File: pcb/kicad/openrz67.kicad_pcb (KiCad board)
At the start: 2 copper layers, 48 x 22 mm, 57 parts, among them J1 GPIO header, U1 ESP32-C3FH4, U2 TPS63031DSKR, U3 BQ25185DLHR, U4 S4B-XH-A(LF)(SN), U5 TLP172AM, U6 TLP172AM, X1 40MHz, X2 32.768kHz

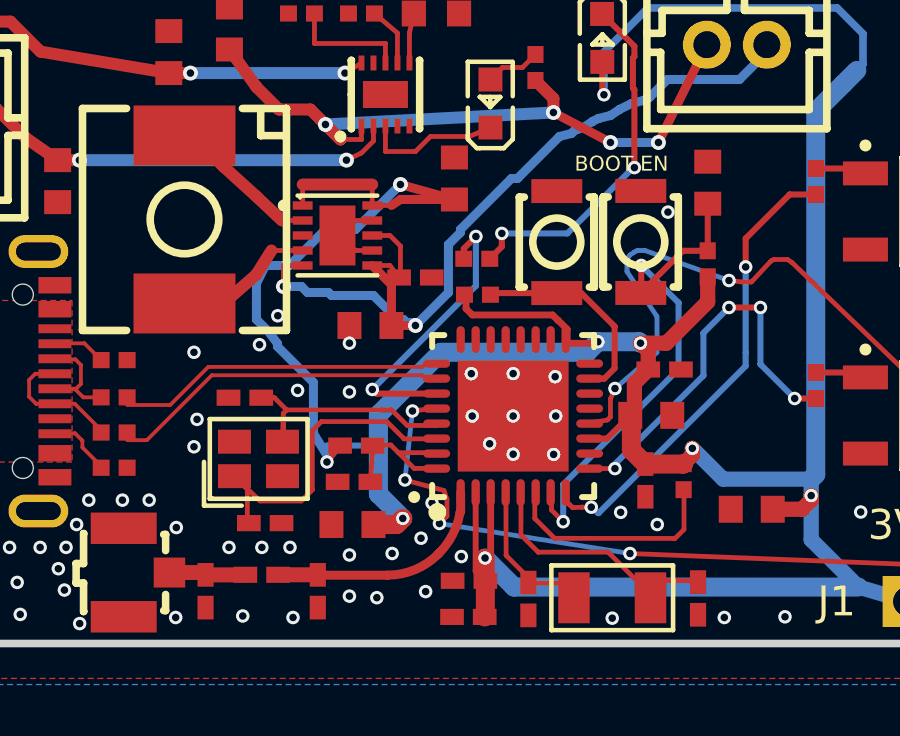
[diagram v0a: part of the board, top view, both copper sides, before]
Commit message: PCB: routing pass — U2 EP vias + solid GND, VCC feed off U2 pad, GPIO21 jog away from LNA_IN
- U2 exposed pad: 4 GND vias (0.45/0.25); U2 and USB1 pads 1/12 solid zone
  connect, starved_thermal warnings gone
- B.Cu VCC feed from U2 output routed around the west side of U2 instead of
  under its pad; SW1/SW2 pad exits 0.254 mm
- GPIO21 F.Cu jog next to U1 pin 1 (LNA_IN) moved 0.75 mm west (0.21 -> 0.79 mm
  to the RF trace); two GND stitching vias relocated
- DRC: 0 errors, 0 unconnected; B.Cu ground under U1 keeps its channel
- README: via 0.45/0.25, warnings table, changelog; out/ regenerated
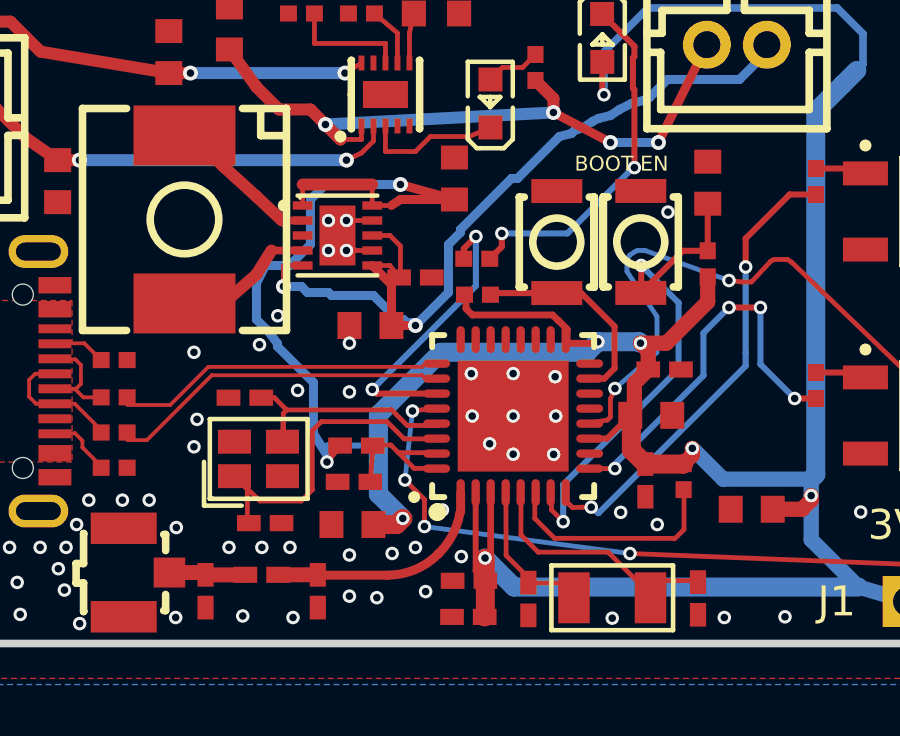
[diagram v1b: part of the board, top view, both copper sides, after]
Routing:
- net VCC: track 116.6 -> 117.5 mm
- net GND: vias 74 -> 78
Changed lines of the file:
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@@
 			)
 		)
+		(zone_connect 2)
 		(attr smd)
 		(duplicate_pad_numbers_are_jumpers no)
@@
 			(layers "F.Cu" "F.Mask" "F.Paste")
 			(net "GND")
+			(zone_connect 2)
 		)
 		(pad "2" smd rect
@@
 			(layers "F.Cu" "F.Mask" "F.Paste")
 			(net "GND")
+			(zone_connect 2)
 		)
 		(pad "13" thru_hole oval
@@
 	)
 	(via
-		(at 138.1865 108.4905)
+		(at 138 108.8)
 		(size 0.45)
 		(drill 0.25)
@@
 	)
 	(via
+		(at 135.7 98.9)
+		(size 0.45)
+		(drill 0.25)
+		(layers "F.Cu" "B.Cu")
+		(net "GND")
+	)
+	(via
 		(at 121.3715 101.735)
 		(size 0.45)
@@
 	)
 	(via
-		(at 138.5525 107.3195)
+		(at 135.1 98.9)
+		(size 0.45)
+		(drill 0.25)
+		(layers "F.Cu" "B.Cu")
+		(net "GND")
+	)
+	(via
+		(at 138.9 107.55)
 		(size 0.45)
 		(drill 0.25)
@@
 	)
 	(via
+		(at 135.1 97.9)
+		(size 0.45)
+		(drill 0.25)
+		(layers "F.Cu" "B.Cu")
+		(net "GND")
+	)
+	(via
 		(at 150.3175 111.11)
 		(size 0.45)
@@
 	)
 	(via
+		(at 135.7 97.9)
+		(size 0.45)
+		(drill 0.25)
+		(layers "F.Cu" "B.Cu")
+		(net "GND")
+	)
+	(via
 		(at 121.219 102.7)
 		(size 0.45)
@@
 	)
 	(segment
+		(start 134.5 97.2)
+		(end 134.5 98.7)
+		(width 0.3)
+		(layer "B.Cu")
+		(net "VCC")
+	)
+	(segment
 		(start 136.764 107.018)
 		(end 136.764 104.3765)
@@
 	)
 	(segment
-		(start 137.5 96.7)
-		(end 136 98.2)
+		(start 134.6 103.3)
+		(end 134.6 105)
 		(width 0.3)
 		(layer "B.Cu")
@@
 	)
 	(segment
-		(start 134.6 103.3)
-		(end 134.6 105)
+		(start 137.5 96.7)
+		(end 135 96.7)
 		(width 0.3)
 		(layer "B.Cu")
@@
 	)
 	(segment
-		(start 136 98.2)
-		(end 135 98.2)
-		(width 0.3)
-		(layer "B.Cu")
-		(net "VCC")
-	)
-	(segment
 		(start 134.6 105)
 		(end 135.1 105.8)
@@
 	)
 	(segment
-		(start 135 98.2)
-		(end 133.8 99.4)
+		(start 135 96.7)
+		(end 134.5 97.2)
 		(width 0.3)
 		(layer "B.Cu")
@@
 	)
 	(segment
+		(start 134.5 98.7)
+		(end 133.8 99.4)
+		(width 0.3)
+		(layer "B.Cu")
+		(net "VCC")
+	)
+	(segment
 		(start 129.826 104.0495)
 		(end 131.095 102.78)
@@
 		(start 134.24 97.9)
 		(end 133.55 97.9)
-		(width 0.16)
+		(width 0.254)
 		(layer "F.Cu")
 		(net "SW2")
@@
 		(start 134.24 98.9)
 		(end 133.199999 98.9)
-		(width 0.16)
+		(width 0.254)
 		(layer "F.Cu")
 		(net "SW1")
@@
 	)
 	(segment
-		(start 138.95 106.9)
-		(end 139.05 107.2)
-		(width 0.16)
-		(layer "F.Cu")
-		(net "GPIO21")
-	)
-	(segment
 		(start 138.7 104.15)
 		(end 137.9 104.25)
@@
 	)
 	(segment
-		(start 139.05 107.2)
-		(end 139.05 107.75)
+		(start 138.3 107.2)
+		(end 138.3 108.1)
 		(width 0.16)
 		(layer "F.Cu")
@@
 	)
 	(segment
-		(start 139.05 107.75)
-		(end 138.8 108)
-		(width 0.16)
-		(layer "F.Cu")
-		(net "GPIO21")
-	)
-	(segment
 		(start 137.65 106.55)
-		(end 138.95 106.9)
+		(end 138.3 107.2)
 		(width 0.16)
 		(layer "F.Cu")
@@
 	)
 	(via
-		(at 138.8 108)
+		(at 137.65 106.55)
 		(size 0.45)
 		(drill 0.25)
@@
 	)
 	(via
-		(at 137.65 106.55)
+		(at 138.3 108.1)
 		(size 0.45)
 		(drill 0.25)
@@
 	)
 	(segment
-		(start 138.8 108)
+		(start 138.3 108.1)
 		(end 145.15 109)
 		(width 0.16)

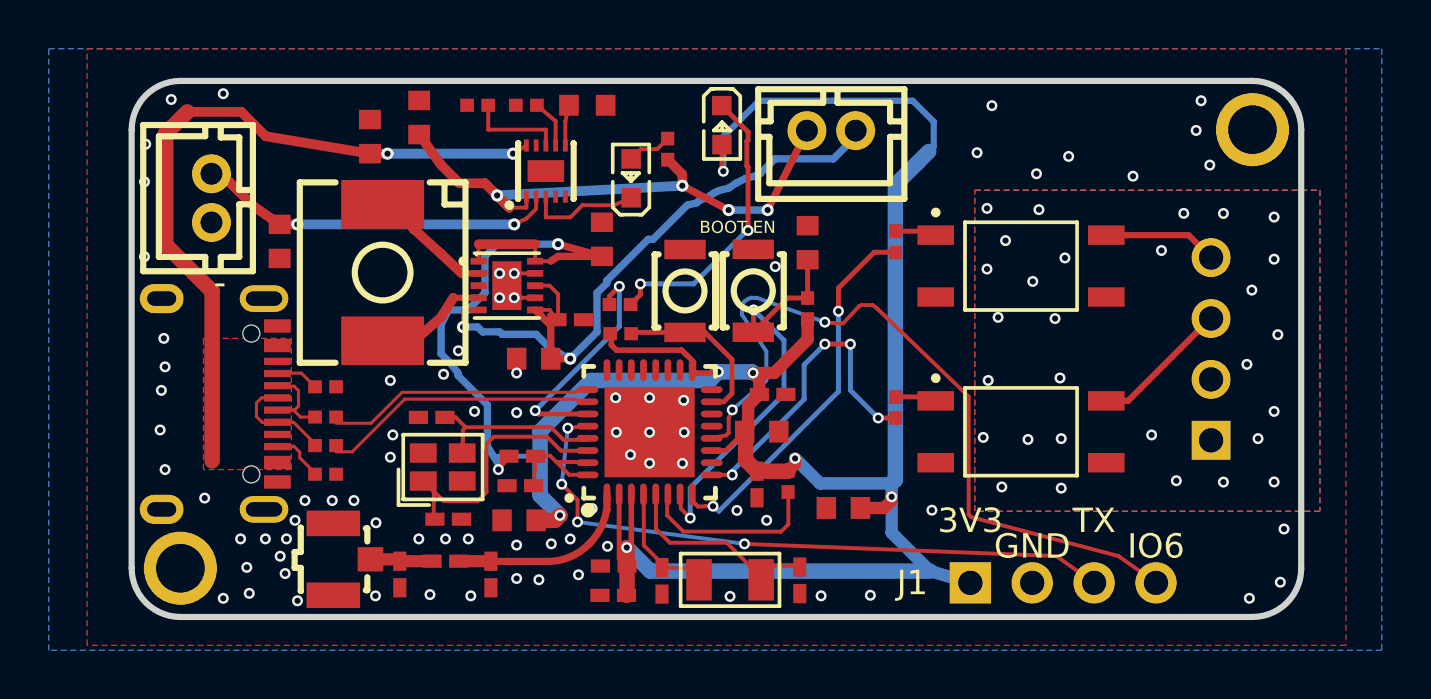
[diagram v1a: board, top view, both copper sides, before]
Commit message: PCB: review fixes — C23 at U2 VIN, GND necks opened, GPIO21 single B.Cu run, U3 EP vias
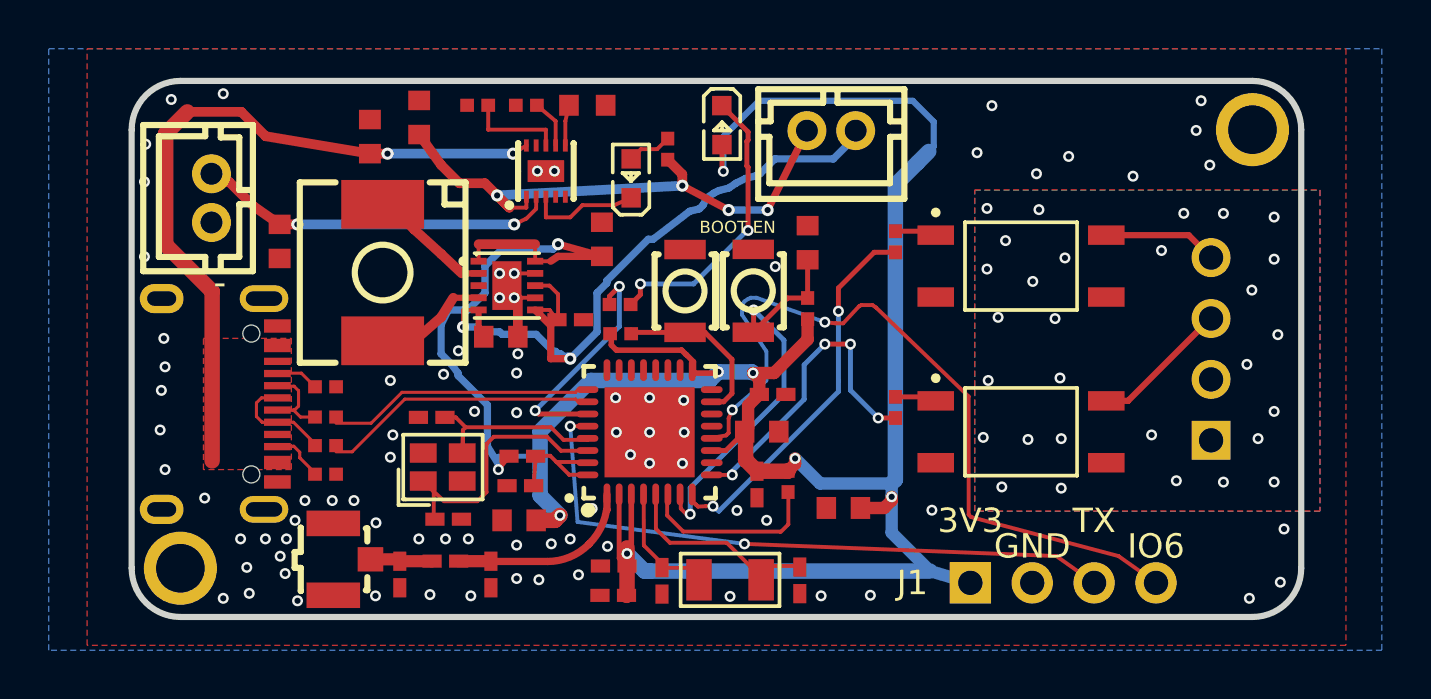
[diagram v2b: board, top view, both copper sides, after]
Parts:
- moved C23 1.62 mm to (135.2, 100.5), turned to 180 degrees
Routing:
- net GND: track 1.40 -> 2.90 mm, vias 78 -> 81
- net SW_SYS: track 29.1 -> 30.3 mm
- net GPIO21: track 26.6 -> 26.3 mm, vias 4 -> 2

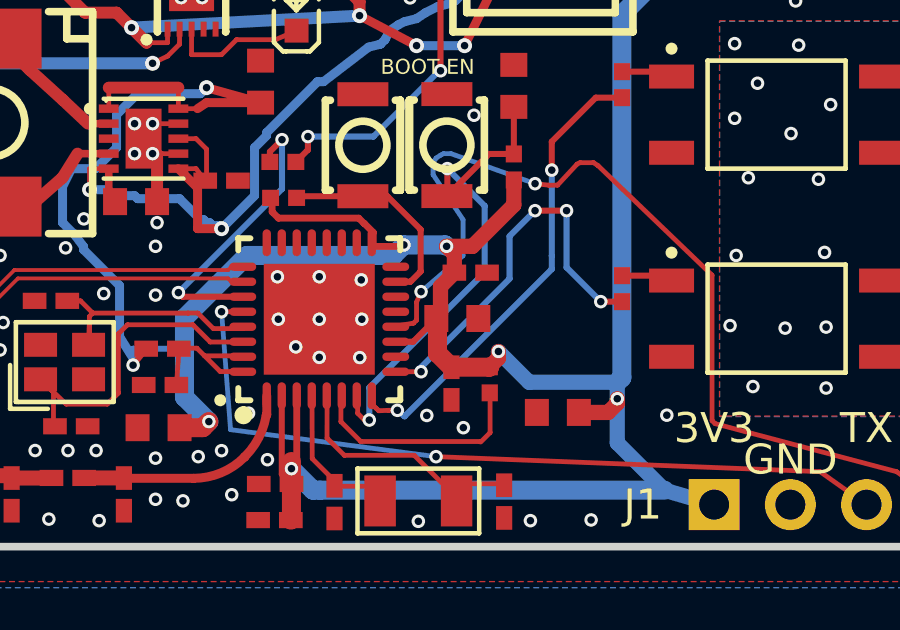
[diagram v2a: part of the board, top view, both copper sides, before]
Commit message: PCB: R23 10k pull-up on GPIO8 (strapping pin was floating); C29 +0.55 mm, GPIO6 via moved, VCC artery on x 25.709
GPIO8 needs to be high for Joint Download Boot and has no internal pull;
rev 1 and the ordered rev 2 leave it floating behind a no-connect flag.
Also adds the 2026-09-10 design review and its adversarial counter-read
under notes/. VDD_SPI 1 uF not added: no room on the top side (README).
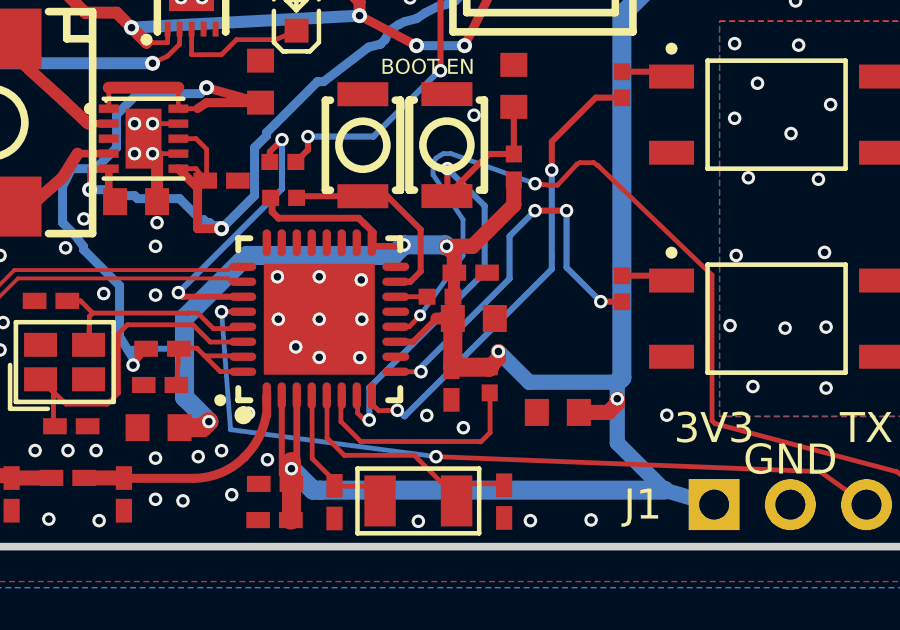
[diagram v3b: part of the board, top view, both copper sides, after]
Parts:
- added R23: 10kΩ, openrz67:R0402, F.Cu at (145.3, 103.7)
- moved C29 0.55 mm to (146.4, 104.4)
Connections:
- U1 pad 14: unconnected-(U1-GPIO8-Pad14) -> GPIO8
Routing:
- net GPIO8: track 0.00 -> 1.04 mm

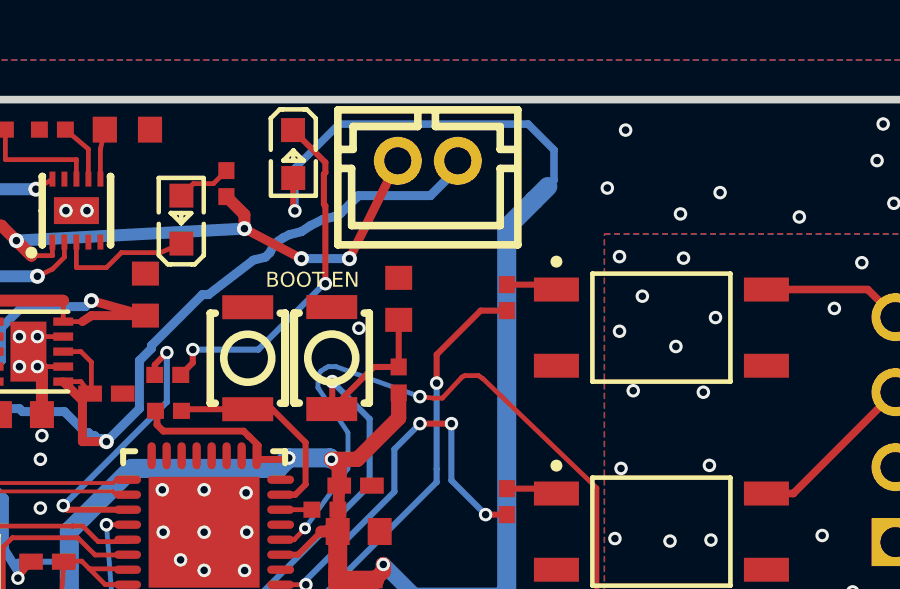
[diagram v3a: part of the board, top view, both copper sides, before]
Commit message: PCB rev 3: battery voltage sense on GPIO3, S2 relay moved to GPIO6
R24/R25 1 MΩ + C32 100 nF under S3 divide SW_SYS (switched cell voltage; BQ25185
SYS voltage on USB) into GPIO3/ADC1_CH3 through the old S2_DRV copper. S2_DRV now
comes from GPIO6 (pin 12), fed off the existing GPIO6 track at (150.55, 99.3), so
J1 pin 4 carries the S2 drive. Every other spare pin was boxed in; BAT+ was
unreachable from U1. DRC 0 errors / 0 unconnected (two new courtyard warnings),
ERC unchanged, title block rev 3. Firmware todo for rev 3 in pcb/kicad/README.md;
src/ still targets rev 2.
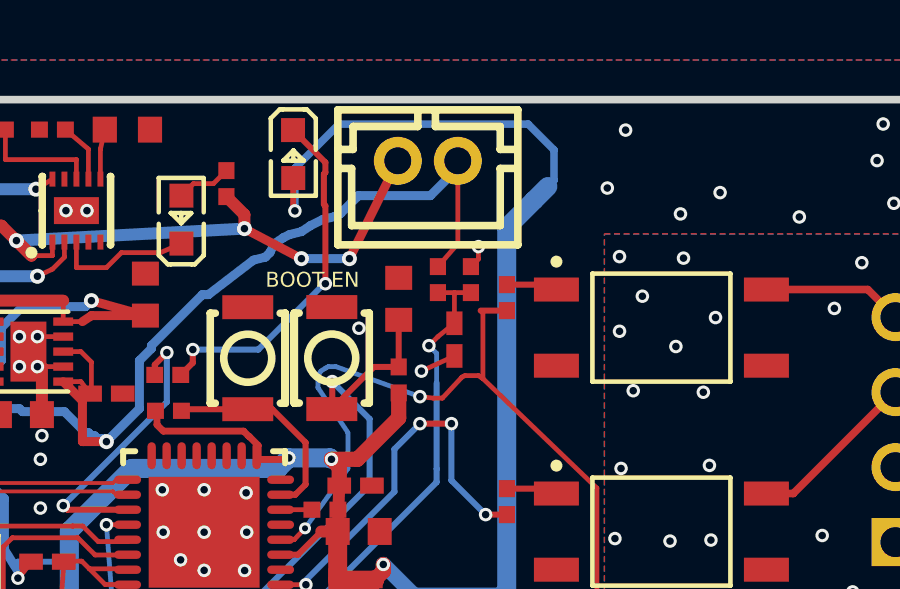
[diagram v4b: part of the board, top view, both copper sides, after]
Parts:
- added C32: 100nF, openrz67:C0402, F.Cu at (149.6, 98.0)
- added R24: 1MΩ, openrz67:R0402, F.Cu at (149.1, 96.0)
- added R25: 1MΩ, openrz67:R0402, F.Cu at (150.2, 96.0)
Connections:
- J1 pad 4: GPIO6 -> S2_DRV
- U1 pad 12: GPIO6 -> S2_DRV
- U1 pad 8: S2_DRV -> VBAT_SENSE
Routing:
- net GPIO6: track 31.4 -> 0.00 mm, vias 2 -> 0
- net S2_DRV: track 15.7 -> 34.6 mm
- net VBAT_SENSE: track 0.00 -> 16.4 mm, vias 0 -> 2
- net SW_SYS: track 30.3 -> 34.1 mm
- net GND: track 2.90 -> 4.88 mm, vias 81 -> 83

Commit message: PCB rev 3: J1 shrinks to 1x3 (3V3, GND, TX); GPIO6 track to the old pin 4 and IO6 silk removed
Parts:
- J1: footprint openrz67:PinHeader_1x04_P2.54mm_Vertical -> openrz67:PinHeader_1x03_P2.54mm_Vertical
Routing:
- net S2_DRV: track 34.6 -> 16.1 mm
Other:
- board text removed: "IO6"
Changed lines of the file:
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@@
 		)
 	)
-	(footprint "openrz67:PinHeader_1x04_P2.54mm_Vertical"
+	(footprint "openrz67:PinHeader_1x03_P2.54mm_Vertical"
 		(layer "F.Cu")
 		(at 154.42 110.6 90)
-		(descr "Through hole straight pin header, 1x04, 2.54mm pitch, single row")
-		(tags "Through hole pin header THT 1x04 2.54mm single row")
+		(descr "Through hole straight pin header, 1x03, 2.54mm pitch, single row")
+		(tags "Through hole pin header THT 1x03 2.54mm single row")
 		(property "Reference" "J1"
 			(at 0 -2.38 0)
@@
 		)
 		(property "Value" "GPIO header"
-			(at 0 10 0)
+			(at 0 7.5 0)
 			(layer "F.Fab")
 			(effects
@@
 			)
 		)
-		(property "Description" "1x4 2.54 mm pin header, not populated by the assembler"
+		(property "Description" "1x3 2.54 mm pin header, not populated by the assembler"
 			(at 0 0 0)
 			(layer "F.Fab")
@@
 		(fp_rect
 			(start -1.77 -1.77)
-			(end 1.77 9.39)
+			(end 1.77 6.85)
 			(stroke
 				(width 0.05)
@@
 		(fp_line
 			(start 1.27 -1.27)
-			(end 1.27 8.89)
+			(end 1.27 6.35)
 			(stroke
 				(width 0.1)
@@
 		)
 		(fp_line
-			(start 1.27 8.89)
-			(end -1.27 8.89)
+			(start 1.27 6.35)
+			(end -1.27 6.35)
 			(stroke
 				(width 0.1)
@@
 		)
 		(fp_line
-			(start -1.27 8.89)
+			(start -1.27 6.35)
 			(end -1.27 -0.635)
 			(stroke
@@
 		)
 		(fp_text user "${REFERENCE}"
-			(at 0 3.81 90)
+			(at 0 2.54 90)
 			(layer "F.Fab")
 			(effects
@@
 			(net "GPIO21")
 		)
-		(pad "4" thru_hole circle
-			(at 0 7.62 90)
-			(size 1.7 1.7)
-			(drill 1)
-			(layers "*.Cu" "*.Mask")
-			(remove_unused_layers no)
-			(net "S2_DRV")
-		)
 		(embedded_fonts no)
-		(model "${KICAD10_3DMODEL_DIR}/Connector_PinHeader_2.54mm.3dshapes/PinHeader_1x04_P2.54mm_Vertical.step"
+		(model "${KICAD10_3DMODEL_DIR}/Connector_PinHeader_2.54mm.3dshapes/PinHeader_1x03_P2.54mm_Vertical.step"
 			(offset
 				(xyz 0 0 0)
@@
 		)
 	)
-	(gr_text "IO6"
-		(at 162.04 109.1 0)
-		(layer "F.SilkS")
-		(effects
-			(font
-				(size 1 1)
-				(thickness 0.15)
-			)
-		)
-	)
 	(gr_text "-"
 		(at 123.354 98.9025 0)
@@
 	)
 	(segment
-		(start 154.35 102.95)
-		(end 154.35 107.8)
-		(width 0.16)
-		(layer "F.Cu")
-		(net "S2_DRV")
-	)
-	(segment
 		(start 144.257 104.669)
 		(end 144.62 104.29)
@@
 	)
 	(segment
-		(start 154.35 107.8)
-		(end 154.45 107.9)
-		(width 0.16)
-		(layer "F.Cu")
-		(net "S2_DRV")
-	)
-	(segment
 		(start 149.85 99.25)
 		(end 149.95 99.2)
@@
 		(layer "F.Cu")
 		(net "S2_DRV")
-	)
-	(segment
-		(start 150.55 99.3)
-		(end 154.35 102.95)
-		(width 0.16)
-		(layer "F.Cu")
-		(net "S2_DRV")
-	)
-	(segment
-		(start 154.45 107.9)
-		(end 160.5 109.5)
-		(width 0.16)
-		(layer "F.Cu")
-		(net "S2_DRV")
-	)
-	(segment
-		(start 160.5 109.5)
-		(end 162.05 110.6)
-		(width 0.16)
-		(layer "F.Cu")
-		(net "S2_DRV")

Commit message: PCB rev 3: reverse-battery P-FET Q3, C24 at the buck-boost output, EP paste windows, 0.8 mm RF line, review notes
Review round 2026-09-25 (pcb/kicad/notes/review-2026-09-25.md):
- Q3 AO3401A (SOT-23, C15127) between BAT1 pin 1 (new net BAT_CELL) and BAT+;
  gate to GND. VBUS moved to B.Cu under it; BAT+ rerouted west of L3 pad 1.
- C24 to (138.0, 97.0), 1.5 mm from U2 VOUT, with a return GND via.
- U1 exposed pad: no paste on the pad, four 1.5 mm aperture windows; U2/U3
  exposed pads 85 % paste. Same change in the library footprints.
- RF line 0.8 mm from the U.FL pad to C2 (~52 ohm).
- S2_DRV via 0.45/0.25 (no JLCPCB surcharge), nudged into the free slot.
- Bottom silk v3, '+' at BAT1 pin 1, schematic note for rev 3 pins.
- README: rev 3 section, accepted warnings (13 courtyard), fab notes, the
  findings accepted without a change and why.
DRC 0 errors / 16 warnings, ERC 0 errors / 15 warnings, parity clean.
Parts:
- added Q3: AO3401A, openrz67:SOT-23, F.Cu at (126.9, 91.7)
- moved C24 1.39 mm to (138.0, 97.0)
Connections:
- BAT1 pad 1: BAT+ -> BAT_CELL
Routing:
- net BAT+: track 14.8 -> 18.7 mm
- net BAT_CELL: track 0.00 -> 3.65 mm
- net VCC: track 117.2 -> 114.1 mm
- net GND: track 4.88 -> 6.46 mm, vias 83 -> 85
- net VBUS: track 30.0 -> 30.5 mm, vias 2 -> 3
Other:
- board text added: "+"
- board text added: "OpenRZ67 Trigger v3 2026-09"
- board text removed: "OpenRZ67 Trigger v2 2026-09"
